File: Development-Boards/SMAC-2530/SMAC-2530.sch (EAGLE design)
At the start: 42 parts, among them CON1 CC_DEBUGGER, IC1 CC2530, IC2 FT230XQ, IC3 TPS732XX, Q1 32MHz

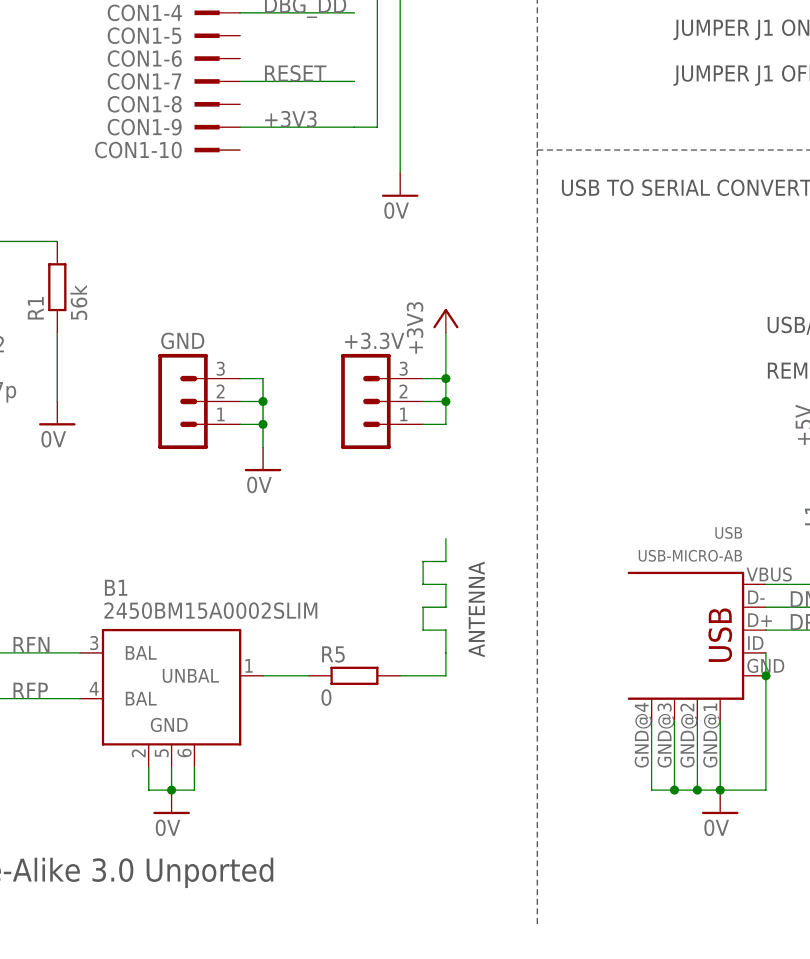
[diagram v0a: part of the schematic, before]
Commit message: SMAC-2530 release v1.1, better antenna grounding, removed R0 jumper
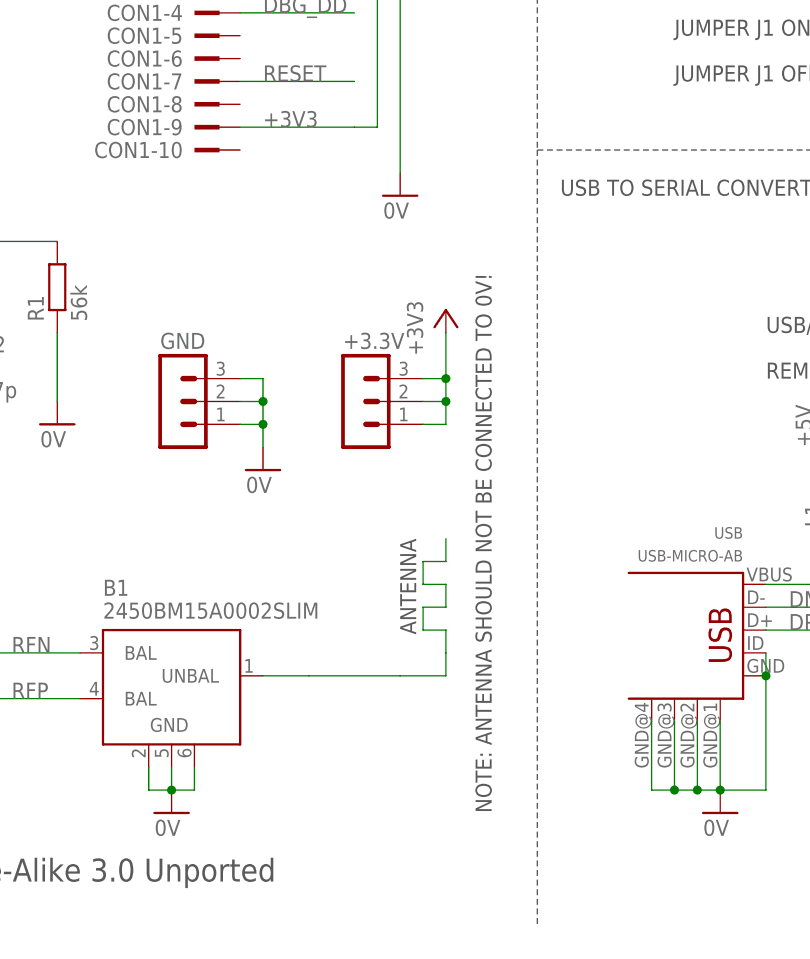
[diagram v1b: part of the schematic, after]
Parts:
- removed R5: 0, resistor:R-EU_R0603K
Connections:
- removed net N$6: B1.UNBAL, R5.1
- net 0V: now also B1.UNBAL; no longer R5.2
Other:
- note added: "NOTE: ANTENNA SHOULD NOT BE CONNECTED TO 0V!"
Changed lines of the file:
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@@
 <part name="GND7" library="supply1" deviceset="0V" device=""/>
 <part name="+3V2" library="supply1" deviceset="+3V3" device="" value="+3V3A"/>
-<part name="R5" library="resistor" deviceset="R-EU_" device="R0603K" value="0"/>
 <part name="LCD3310" library="con-lsta" deviceset="FE05-2" device=""/>
 <part name="PORT0" library="con-lstb" deviceset="MA10-1" device=""/>
@@
 <wire x1="12.7" y1="149.86" x2="162.56" y2="149.86" width="0.1524" layer="97" style="shortdash"/>
 <wire x1="162.56" y1="149.86" x2="162.56" y2="104.14" width="0.1524" layer="97" style="shortdash"/>
-<text x="154.94" y="58.42" size="1.778" layer="97" rot="R270">ANTENNA</text>
+<text x="147.32" y="60.96" size="1.778" layer="97" rot="R270">ANTENNA</text>
 <wire x1="162.56" y1="104.14" x2="162.56" y2="17.78" width="0.1524" layer="97" style="shortdash"/>
 <wire x1="162.56" y1="104.14" x2="261.62" y2="104.14" width="0.1524" layer="97" style="shortdash"/>
@@
 <text x="15.24" y="193.04" size="2.54" layer="97">SMAC Project - SMAC-2530 Reference Design</text>
 <text x="127" y="193.04" size="2.54" layer="97">http://smacproject.org</text>
+<text x="157.48" y="30.48" size="1.778" layer="97" rot="R90">NOTE: ANTENNA SHOULD NOT BE CONNECTED TO 0V!</text>
 </plain>
 <instances>
@@
 <instance part="GND7" gate="1" x="121.92" y="30.48"/>
 <instance part="+3V2" gate="G$1" x="35.56" y="68.58"/>
-<instance part="R5" gate="G$1" x="142.24" y="45.72"/>
 <instance part="LCD3310" gate="G$1" x="297.18" y="172.72" smashed="yes" rot="MR180">
 <attribute name="VALUE" x="293.37" y="182.88" size="1.778" layer="96" rot="MR180"/>
@@
 <wire x1="149.86" y1="58.42" x2="152.4" y2="58.42" width="0.1524" layer="91"/>
 <wire x1="152.4" y1="58.42" x2="152.4" y2="60.96" width="0.1524" layer="91"/>
-<pinref part="R5" gate="G$1" pin="2"/>
 <wire x1="147.32" y1="45.72" x2="152.4" y2="45.72" width="0.1524" layer="91"/>
 <wire x1="152.4" y1="45.72" x2="152.4" y2="48.26" width="0.1524" layer="91"/>
+<pinref part="B1" gate="G$1" pin="UNBAL"/>
+<wire x1="137.16" y1="45.72" x2="132.08" y2="45.72" width="0.1524" layer="91"/>
+<wire x1="137.16" y1="45.72" x2="147.32" y2="45.72" width="0.1524" layer="91"/>
 </segment>
 <segment>
@@
 </segment>
 </net>
-<net name="N$6" class="0">
-<segment>
-<pinref part="R5" gate="G$1" pin="1"/>
-<pinref part="B1" gate="G$1" pin="UNBAL"/>
-<wire x1="137.16" y1="45.72" x2="132.08" y2="45.72" width="0.1524" layer="91"/>
-</segment>
-</net>
